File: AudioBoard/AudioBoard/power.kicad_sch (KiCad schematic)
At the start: 0 parts

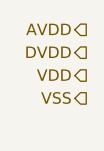
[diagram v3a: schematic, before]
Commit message: added xlr output stage
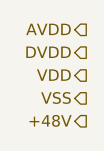
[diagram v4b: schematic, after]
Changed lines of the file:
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@@
+		)
+	)
+	(hierarchical_label "+48V"
+		(shape output)
+		(at 31.75 38.1 180)
+		(effects
+			(font
+				(size 1.27 1.27)
+			)
+			(justify right)
 		)
 	)

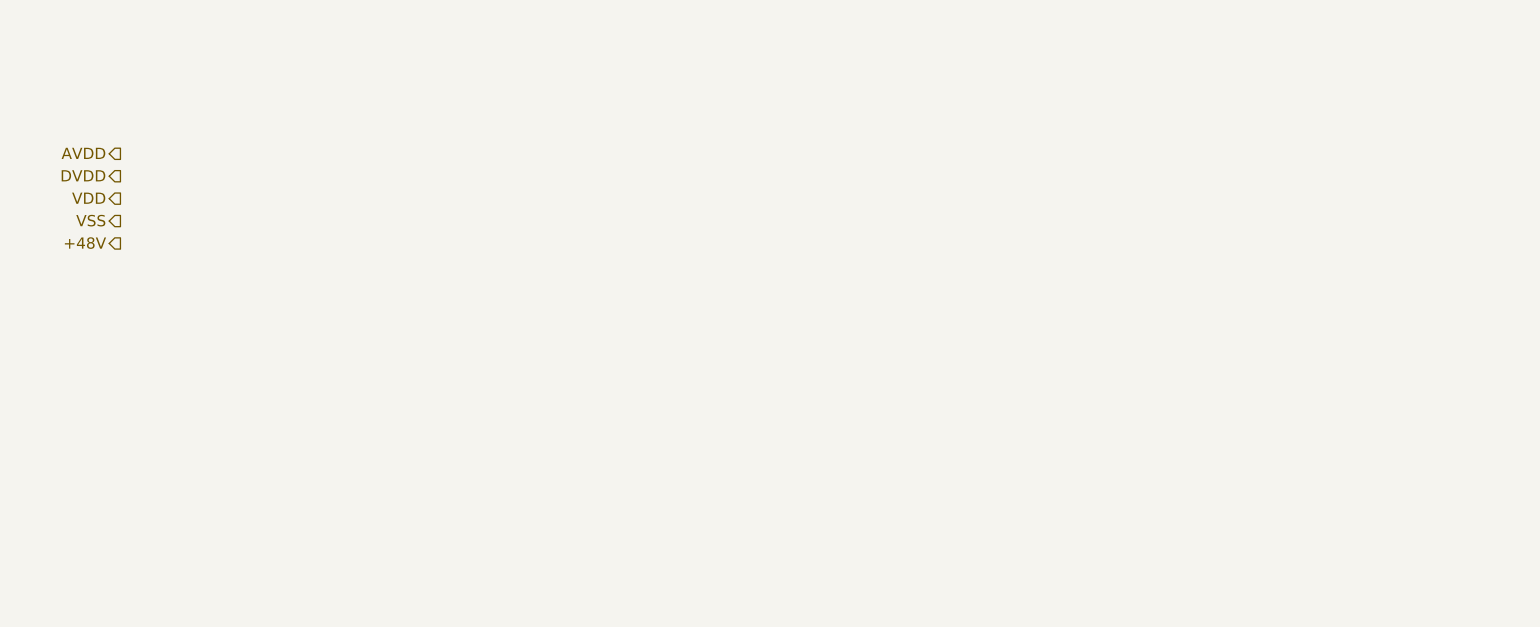
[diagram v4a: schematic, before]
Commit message: added jack IO, headphone amp cirucit
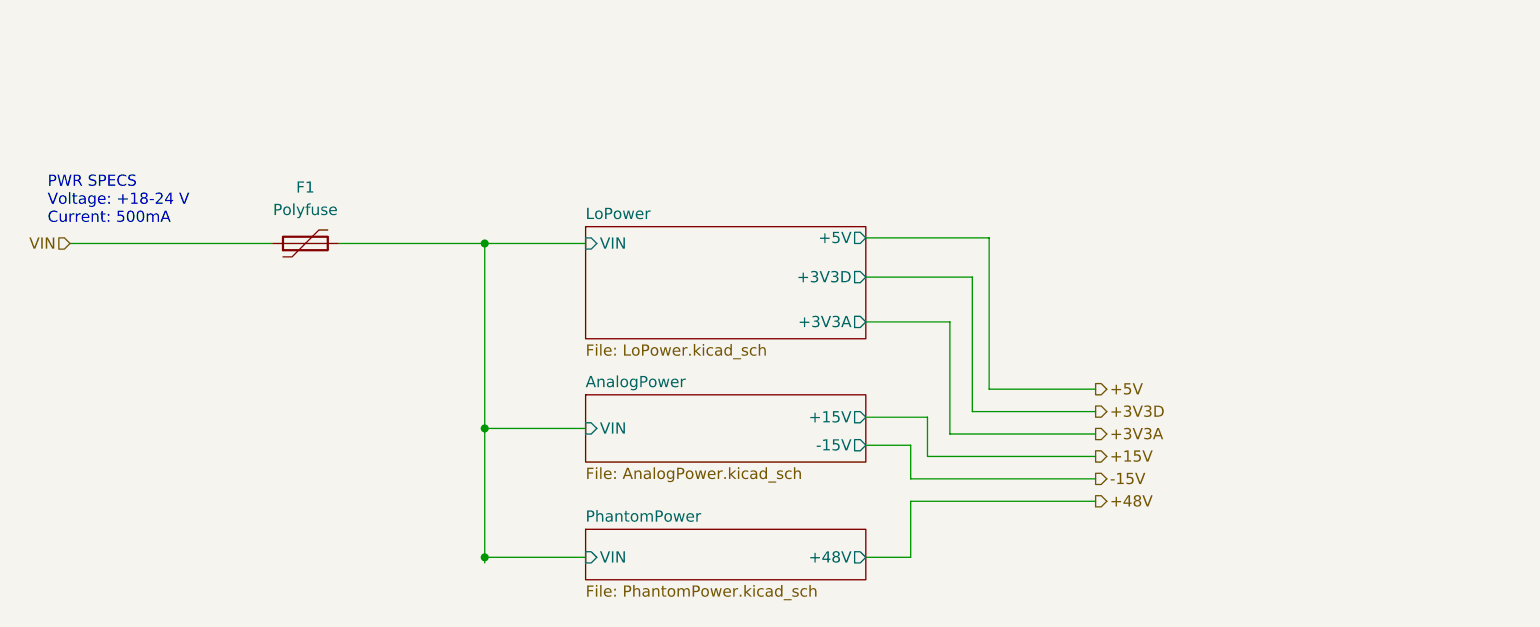
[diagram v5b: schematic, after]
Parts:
- added F1: Polyfuse, symbol Device:Polyfuse
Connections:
- new net AnalogPower/VIN: F1.2
- new net VIN: F1.1
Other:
- added sheet AnalogPower (AnalogPower.kicad_sch)
- added sheet LoPower (LoPower.kicad_sch)
- added sheet PhantomPower (PhantomPower.kicad_sch)
- note added: "PWR SPECS Voltage: +18-24 V Current: 500mA"

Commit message: added pwr sw and headphone out
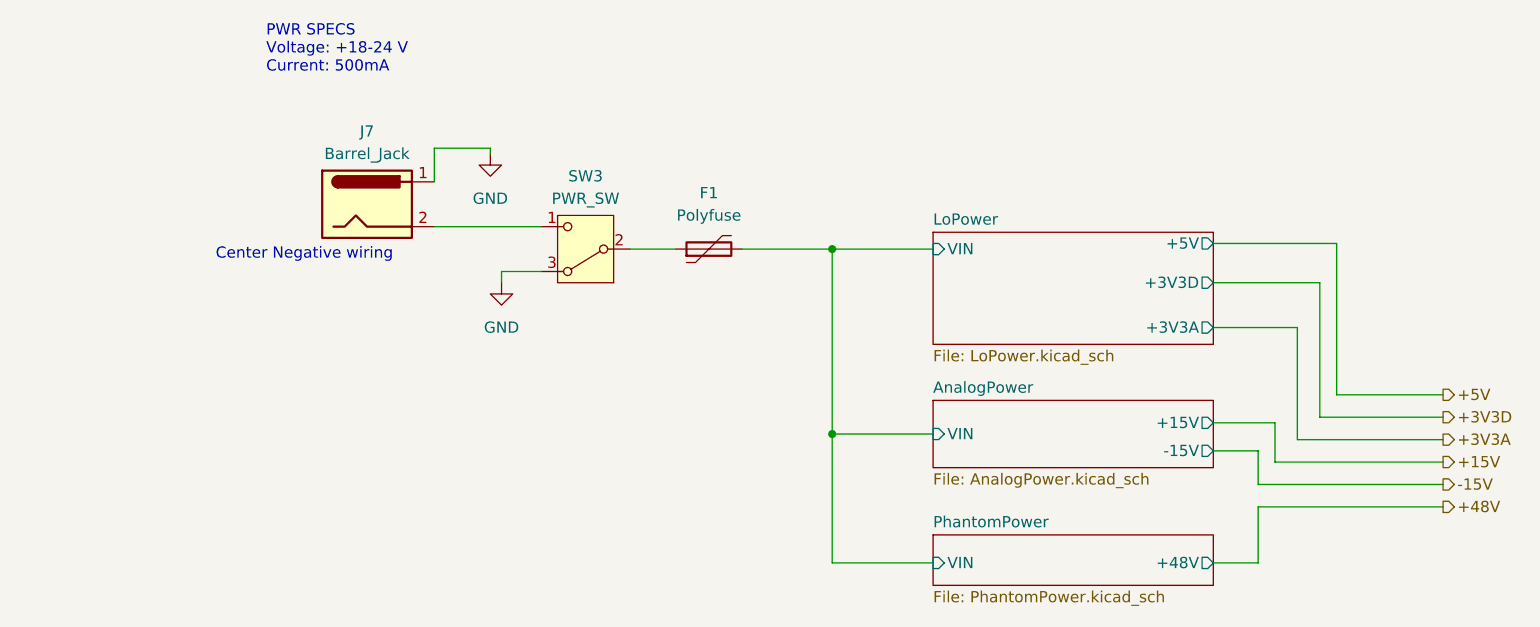
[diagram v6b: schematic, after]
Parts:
- added J7: Barrel_Jack, Connector_BarrelJack:BarrelJack_Wuerth_6941xx301002, symbol Connector:Barrel_Jack
- added SW3: PWR_SW, haoyu:SS-12D28G7, symbol Switch:SW_SPDT_321
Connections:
- net VIN: no longer names the net of F1.1
- net VIN: now also SW3.2 (B)
- new net: J7.2, SW3.1 (C)
- new net GND: J7.1, SW3.3 (A)
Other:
- note added: "Center Negative wiring"
- moved on the sheet: F1

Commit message: added lcscpart to components and assigned footprints
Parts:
- J7: JLCPCB (none) -> C3010533; LCSC Part (none) -> C3010533
- SW3: JLCPCB (none) -> C2884748; LCSC Part (none) -> C2884748
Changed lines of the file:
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@@
+			)
+		)
+		(property "JLCPCB" "C2884748"
+			(at 84.455 38.735 0)
+			(hide yes)
+			(show_name no)
+			(do_not_autoplace no)
+			(effects
+				(font
+					(size 1.27 1.27)
+				)
+			)
+		)
+		(property "LCSC Part" "C2884748"
+			(at 84.455 38.735 0)
+			(hide yes)
+			(show_name no)
+			(do_not_autoplace no)
+			(effects
+				(font
+					(size 1.27 1.27)
+				)
 			)
 		)
@@
 			(at 59.69 33.655 0)
 			(hide yes)
+			(show_name no)
+			(do_not_autoplace no)
+			(effects
+				(font
+					(size 1.27 1.27)
+				)
+			)
+		)
+		(property "JLCPCB" "C3010533"
+			(at 59.69 33.655 0)
+			(hide yes)
+			(show_name no)
+			(do_not_autoplace no)
+			(effects
+				(font
+					(size 1.27 1.27)
+				)
+			)
+		)
+		(property "LCSC Part" "C3010533"
+			(at 59.69 33.655 0)
+			(hide yes)
